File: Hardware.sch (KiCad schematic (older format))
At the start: 25 parts, among them J1 Power, J11 RJ45-NoShield, J2 RJ45-Dual, J3 SWD_Conn, J4 ESP_Conn, J5 Spare_Conn, J6 Power_Conn, U1 STM32F042G6Ux, U2 MCP9700T-ETT, U3 MCP9700T-ETT, Y1 8MHz

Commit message: Added Address-Selector
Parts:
- J5: footprint Connector_PinHeader_2.54mm:PinHeader_1x07_P2.54mm_Vertical -> Connector_PinHeader_2.54mm:PinHeader_1x03_P2.54mm_Vertical; symbol Connector_Specialized:Conn_01x07_Female -> Connector_Specialized:Conn_01x03_Female
- gave numbers to parts that had none: 1
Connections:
- net SPARE1: now also R1.1, U1.1 (PB8/CAN_RX/CEC/I2C1_SCL); no longer U1.15 (PB1/ADC_IN9)
- net SPARE2: now also J4.3 (Pin_3); no longer U1.25 (PB4/SPI1_MISO)
- net SPARE3: now also J4.5 (Pin_5); no longer U1.26 (PB5/I2C1_SMBA/SPI1_MOSI)
- removed net SPARE4: J5.4 (Pin_4), R1.1, U1.1 (PB8/CAN_RX/CEC/I2C1_SCL)
- net SPARE5 renamed ADDR
- net ADDR: no longer J5.5 (Pin_5)
- removed net SPARE6: J4.3 (Pin_3), J5.6 (Pin_6)
- removed net SPARE7: J4.5 (Pin_5), J5.7 (Pin_7)
- new net PULLM: U1.26 (PB5/I2C1_SMBA/SPI1_MOSI)
- new net S_CLK: U1.25 (PB4/SPI1_MISO)
- new net S_SER: U1.15 (PB1/ADC_IN9)
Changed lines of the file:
@@
 TEMP2
 Text GLabel 2350 2350 0    60   Input ~ 0
+S_SER
+Text GLabel 2200 2950 0    60   Input ~ 0
 SPARE1
-Text GLabel 2300 2550 0    60   Input ~ 0
-SPARE2
-Text GLabel 2250 2650 0    60   Input ~ 0
-SPARE3
-Text GLabel 2200 2950 0    60   Input ~ 0
-SPARE4
-Text GLabel 6250 1750 2    60   Input ~ 0
-SPARE5
 Text Notes 8900 3800 0    120  ~ 0
 Power
 $Sheet
-S 9725 2200 950  700
+S 9725 2575 950  700
 U 5A846A20
 F0 "CAN" 60
 F1 "CAN.sch" 60
-F2 "5V" I L 9725 2250 60
-F3 "3V3" I L 9725 2400 60
-F4 "CAN_TX" I L 9725 2550 60
-F5 "CAN_RX" O L 9725 2700 60
-F6 "GND" I L 9725 2850 60
-F7 "CAN_H" B R 10675 2400 60
-F8 "CAN_L" B R 10675 2700 60
+F2 "5V" I L 9725 2625 60
+F3 "3V3" I L 9725 2775 60
+F4 "CAN_TX" I L 9725 2925 60
+F5 "CAN_RX" O L 9725 3075 60
+F6 "GND" I L 9725 3225 60
+F7 "CAN_H" B R 10675 2775 60
+F8 "CAN_L" B R 10675 3075 60
 $EndSheet
 $Sheet
-S 9725 1100 950  700
+S 9725 975  950  1300
 U 5A84CF44
 F0 "DMX" 60
 F1 "DMX.sch" 60
-F2 "5V" I L 9725 1150 60
-F3 "UART_TX" I L 9725 1450 60
-F4 "UART_RX" O L 9725 1600 60
-F5 "GND" I L 9725 1750 60
-F6 "DMX_A" B R 10675 1300 60
-F7 "DMX_B" B R 10675 1600 60
-F8 "UART_SE" I L 9725 1300 60
+F2 "5V" I L 9725 1025 60
+F3 "UART_TX" I L 9725 1325 60
+F4 "UART_RX" O L 9725 1475 60
+F5 "GND" I L 9725 2225 60
+F6 "DMX_A" B R 10675 1175 60
+F7 "DMX_B" B R 10675 1475 60
+F8 "UART_SE" I L 9725 1175 60
+F9 "S_SER" I L 9725 1625 60
+F10 "S_CLK" I L 9725 1775 60
+F11 "PULLM" I L 9725 1925 60
+F12 "ADDR" O L 9725 2075 60
 $EndSheet
 $Comp
 L power:GND #PWR034
 U 1 1 5A85098C
-P 9675 2950
-F 0 "#PWR034" H 9675 2700 50  0001 C CNN
-F 1 "GND" H 9675 2800 50  0000 C CNN
-F 2 "" H 9675 2950 50  0001 C CNN
-F 3 "" H 9675 2950 50  0001 C CNN
-	1    9675 2950
+P 9675 3325
+F 0 "#PWR034" H 9675 3075 50  0001 C CNN
+F 1 "GND" H 9675 3175 50  0000 C CNN
+F 2 "" H 9675 3325 50  0001 C CNN
+F 3 "" H 9675 3325 50  0001 C CNN
+	1    9675 3325
 	1    0    0    -1
 $EndComp
@@
 L power:+5V #PWR033
 U 1 1 5A850F4A
-P 9625 1050
-F 0 "#PWR033" H 9625 900 50  0001 C CNN
-F 1 "+5V" H 9625 1190 50  0000 C CNN
-F 2 "" H 9625 1050 50  0001 C CNN
-F 3 "" H 9625 1050 50  0001 C CNN
-	1    9625 1050
+P 9625 925
+F 0 "#PWR033" H 9625 775 50  0001 C CNN
+F 1 "+5V" H 9625 1065 50  0000 C CNN
+F 2 "" H 9625 925 50  0001 C CNN
+F 3 "" H 9625 925 50  0001 C CNN
+	1    9625 925
 	1    0    0    -1
 $EndComp
@@
 L power:+3.3V #PWR032
 U 1 1 5A851B94
-P 9475 2400
-F 0 "#PWR032" H 9475 2250 50  0001 C CNN
-F 1 "+3.3V" H 9475 2540 50  0000 C CNN
-F 2 "" H 9475 2400 50  0001 C CNN
-F 3 "" H 9475 2400 50  0001 C CNN
-	1    9475 2400
-	1    0    0    -1
-$EndComp
-Text GLabel 9575 1300 0    60   Input ~ 0
+P 9475 2775
+F 0 "#PWR032" H 9475 2625 50  0001 C CNN
+F 1 "+3.3V" H 9475 2915 50  0000 C CNN
+F 2 "" H 9475 2775 50  0001 C CNN
+F 3 "" H 9475 2775 50  0001 C CNN
+	1    9475 2775
+	1    0    0    -1
+$EndComp
+Text GLabel 9575 1175 0    60   Input ~ 0
 UART2_SE
-Text GLabel 9525 1450 0    60   Input ~ 0
+Text GLabel 9525 1325 0    60   Input ~ 0
 UART2_TX
-Text GLabel 9475 1600 0    60   Input ~ 0
+Text GLabel 9475 1475 0    60   Input ~ 0
 UART2_RX
-Text GLabel 9625 2550 0    60   Input ~ 0
+Text GLabel 9625 2925 0    60   Input ~ 0
 CAN_TX
-Text GLabel 9575 2700 0    60   Input ~ 0
+Text GLabel 9575 3075 0    60   Input ~ 0
 CAN_RX
 Text Notes 8900 625  0    120  ~ 0
@@
 $EndComp
 Text GLabel 4250 4875 0    60   Input ~ 0
-SPARE6
+SPARE2
 Text GLabel 4200 4975 0    60   Input ~ 0
-SPARE7
+SPARE3
 $Comp
 L Device:R_Small R2
@@
 $EndComp
 $Comp
-L Connector_Specialized:Conn_01x07_Female J5
+L Connector_Specialized:Conn_01x03_Female J5
 U 1 1 5A880979
-P 1825 6000
-F 0 "J5" H 1825 6400 50  0000 C CNN
-F 1 "Spare_Conn" H 1825 5600 50  0000 C CNN
-F 2 "Connector_PinHeader_2.54mm:PinHeader_1x07_P2.54mm_Vertical" H 1825 6000 50  0001 C CNN
-F 3 "" H 1825 6000 50  0001 C CNN
-	1    1825 6000
+P 1825 5800
+F 0 "J5" H 1775 5975 50  0000 C CNN
+F 1 "Spare_Conn" H 1650 5625 50  0000 C CNN
+F 2 "Connector_PinHeader_2.54mm:PinHeader_1x03_P2.54mm_Vertical" H 1825 5800 50  0001 C CNN
+F 3 "" H 1825 5800 50  0001 C CNN
+	1    1825 5800
 	1    0    0    -1
 $EndComp
@@
 Text GLabel 1475 5900 0    60   Input ~ 0
 SPARE3
-Text GLabel 1425 6000 0    60   Input ~ 0
-SPARE4
-Text GLabel 1375 6100 0    60   Input ~ 0
-SPARE5
-Text GLabel 1325 6200 0    60   Input ~ 0
-SPARE6
-Text GLabel 1275 6300 0    60   Input ~ 0
-SPARE7
 Wire Wire Line
 	4100 1250 4200 1250
@@
 	6000 2450 6100 2450
 Wire Wire Line
-	6000 1750 6250 1750
+	6000 1750 6200 1750
 Wire Wire Line
 	2250 2250 2400 2250
@@
 Connection ~ 2350 2950
 Wire Wire Line
-	9675 1750 9675 2850
-Wire Wire Line
-	9675 2850 9725 2850
-Wire Wire Line
-	9675 1750 9725 1750
-Connection ~ 9675 2850
-Wire Wire Line
-	9625 1050 9625 1150
-Wire Wire Line
-	9625 1150 9725 1150
-Connection ~ 9625 1150
-Wire Wire Line
-	9625 2250 9725 2250
-Wire Wire Line
-	9475 2400 9725 2400
-Wire Wire Line
-	9575 1300 9725 1300
-Wire Wire Line
-	9525 1450 9725 1450
-Wire Wire Line
-	9725 1600 9475 1600
-Wire Wire Line
-	9625 2550 9725 2550
-Wire Wire Line
-	9575 2700 9725 2700
+	9675 2225 9675 3225
+Wire Wire Line
+	9675 3225 9725 3225
+Connection ~ 9675 3225
+Wire Wire Line
+	9625 925  9625 1025
+Wire Wire Line
+	9625 1025 9725 1025
+Connection ~ 9625 1025
+Wire Wire Line
+	9625 2625 9725 2625
+Wire Wire Line
+	9475 2775 9725 2775
+Wire Wire Line
+	9575 1175 9725 1175
+Wire Wire Line
+	9525 1325 9725 1325
+Wire Wire Line
+	9725 1475 9475 1475
+Wire Wire Line
+	9625 2925 9725 2925
+Wire Wire Line
+	9575 3075 9725 3075
 Wire Notes Line
 	6725 475  6725 7800
@@
 Wire Wire Line
 	1475 5900 1625 5900
-Wire Wire Line
-	1625 6000 1425 6000
-Wire Wire Line
-	1625 6100 1375 6100
-Wire Wire Line
-	1625 6200 1325 6200
-Wire Wire Line
-	1625 6300 1275 6300
 $Comp
 L power:+3.3V #PWR012
@@
 	1    0    0    -1
 $EndComp
-Text GLabel 10725 1300 2    60   Input ~ 0
+Text GLabel 10725 1175 2    60   Input ~ 0
 DMX_A
 Wire Wire Line
-	10725 1300 10675 1300
-Text GLabel 10725 1600 2    60   Input ~ 0
+	10725 1175 10675 1175
+Text GLabel 10725 1475 2    60   Input ~ 0
 DMX_B
 Wire Wire Line
-	10725 1600 10675 1600
-Text GLabel 10725 2400 2    60   Input ~ 0
+	10725 1475 10675 1475
+Text GLabel 10725 2775 2    60   Input ~ 0
 CAN_H
 Wire Wire Line
-	10725 2400 10675 2400
-Text GLabel 10725 2700 2    60   Input ~ 0
+	10725 2775 10675 2775
+Text GLabel 10725 3075 2    60   Input ~ 0
 CAN_L
 Wire Wire Line
-	10725 2700 10675 2700
+	10725 3075 10675 3075
 Text GLabel 3275 7000 3    60   Input ~ 0
 DMX_A
@@
 	2350 2950 2400 2950
 Wire Wire Line
-	9675 2850 9675 2950
-Wire Wire Line
-	9625 1150 9625 2250
+	9675 3225 9675 3325
+Wire Wire Line
+	9625 1025 9625 2625
 Wire Wire Line
 	7900 6200 7900 6300
@@
 Connection ~ 5125 5700
 $Comp
-L power:GND #PWR?
+L power:GND #PWR0107
 U 1 1 5B544A62
 P 3875 7525
-F 0 "#PWR?" H 3875 7275 50  0001 C CNN
+F 0 "#PWR0107" H 3875 7275 50  0001 C CNN
 F 1 "GND" H 3880 7352 50  0000 C CNN
 F 2 "" H 3875 7525 50  0001 C CNN
@@
 	3575 6825 3575 7400
 $Comp
-L Connector_Generic:Conn_01x03 J?
+L Connector_Generic:Conn_01x03 J10
 U 1 1 5B58C10F
 P 3575 7600
-F 0 "J?" V 3575 7325 50  0000 L CNN
+F 0 "J10" V 3575 7325 50  0000 L CNN
 F 1 "Conn_01x03" V 3675 7350 50  0000 L CNN
 F 2 "" H 3575 7600 50  0001 C CNN
@@
 Wire Wire Line
 	3975 7400 3975 6825
+Wire Wire Line
+	9675 2225 9725 2225
+Text GLabel 9575 1625 0    60   Input ~ 0
+S_SER
+Text GLabel 9525 1775 0    60   Input ~ 0
+S_CLK
+Text GLabel 9475 1925 0    60   Input ~ 0
+PULLM
+Text GLabel 9425 2075 0    60   Input ~ 0
+ADDR
+Wire Wire Line
+	9575 1625 9725 1625
+Wire Wire Line
+	9725 1775 9525 1775
+Wire Wire Line
+	9475 1925 9725 1925
+Wire Wire Line
+	9725 2075 9425 2075
+Text GLabel 2300 2550 0    60   Input ~ 0
+S_CLK
+Text GLabel 2250 2650 0    60   Input ~ 0
+PULLM
+Text GLabel 6200 1750 2    60   Input ~ 0
+ADDR
 Wire Bus Line
 	3175 6725 6400 6725

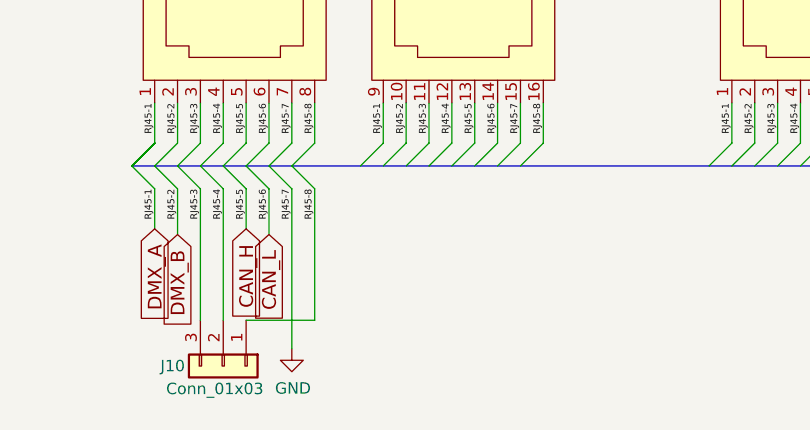
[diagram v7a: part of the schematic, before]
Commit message: Added Connector for DMX
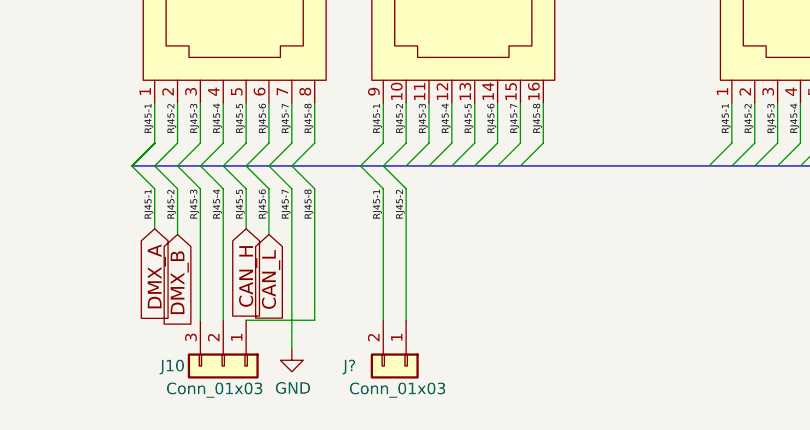
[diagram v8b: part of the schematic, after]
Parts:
- added J?: Conn_01x03, Connector_PinHeader_2.54mm:PinHeader_1x03_P2.54mm_Vertical, symbol Connector_Generic:Conn_01x02
- J10: footprint (none) -> Connector_PinHeader_2.54mm:PinHeader_1x03_P2.54mm_Vertical
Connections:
- net DMX_A: now also J?.2 (Pin_2)
- net DMX_B: now also J?.1 (Pin_1)
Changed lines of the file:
@@
 F 0 "J10" V 3575 7325 50  0000 L CNN
 F 1 "Conn_01x03" V 3675 7350 50  0000 L CNN
-F 2 "" H 3575 7600 50  0001 C CNN
+F 2 "Connector_PinHeader_2.54mm:PinHeader_1x03_P2.54mm_Vertical" H 3575 7600 50  0001 C CNN
 F 3 "~" H 3575 7600 50  0001 C CNN
 	1    3575 7600
@@
 Text GLabel 6200 1750 2    60   Input ~ 0
 ADDR
+$Comp
+L Connector_Generic:Conn_01x02 J?
+U 1 1 5B62FC75
+P 4375 7600
+F 0 "J?" V 4375 7325 50  0000 L CNN
+F 1 "Conn_01x03" V 4475 7350 50  0000 L CNN
+F 2 "Connector_PinHeader_2.54mm:PinHeader_1x03_P2.54mm_Vertical" H 4375 7600 50  0001 C CNN
+F 3 "~" H 4375 7600 50  0001 C CNN
+	1    4375 7600
+	0    1    1    0
+$EndComp
+Entry Wire Line
+	4175 6725 4275 6825
+Entry Wire Line
+	4275 6725 4375 6825
+Wire Wire Line
+	4275 6825 4275 7400
+Wire Wire Line
+	4375 6825 4375 7400
 Wire Bus Line
 	3175 6725 6400 6725
+Text Label 4275 6825 3    30   ~ 0
+RJ45-1
+Text Label 4375 6825 3    30   ~ 0
+RJ45-2
 $EndSCHEMATC
